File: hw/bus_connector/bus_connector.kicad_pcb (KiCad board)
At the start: 2 copper layers, 70 x 36 mm, 12 parts, among them J1 DB9_Top, J2 DB9_Right, J3 DB9_Left

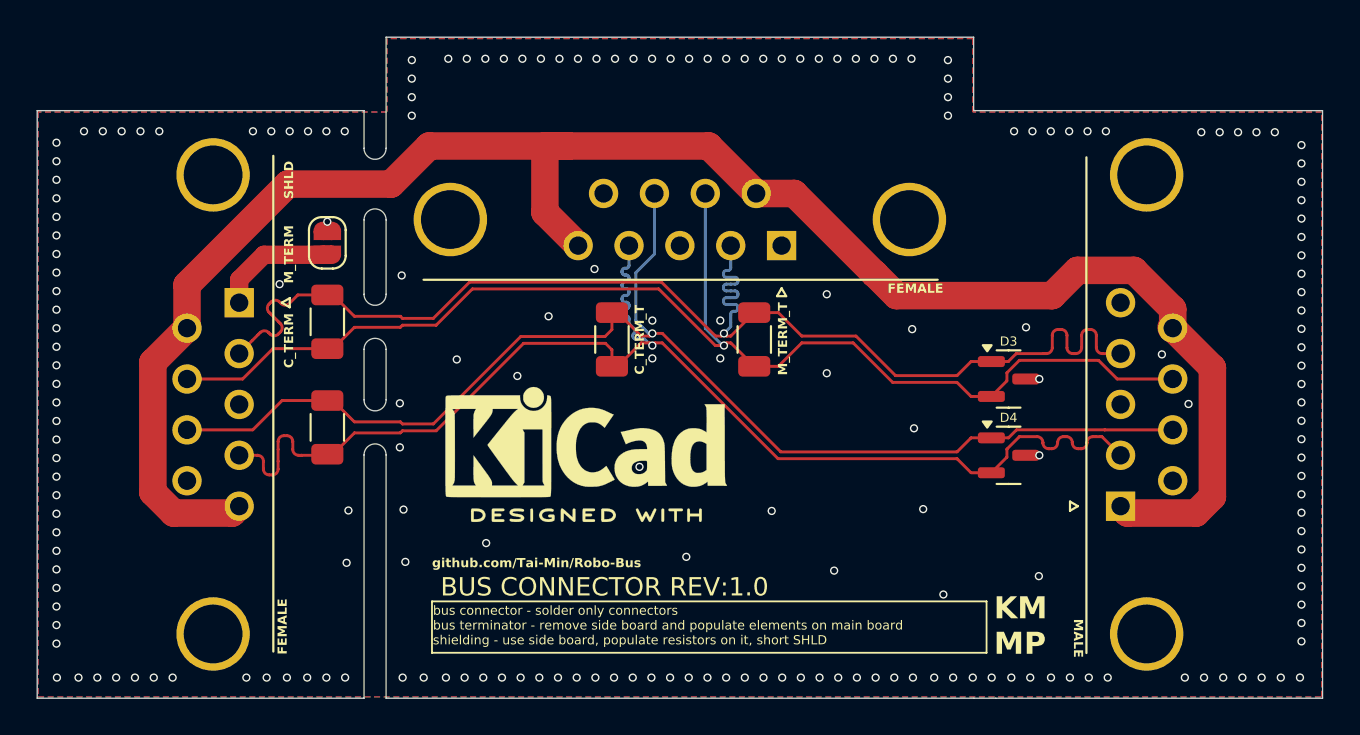
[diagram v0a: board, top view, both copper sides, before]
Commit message: Fix silkscreen, fix thermal error, add via array
Signed-off-by: Mateusz Pająk <22417805+Tai-Min@users.noreply.github.com>
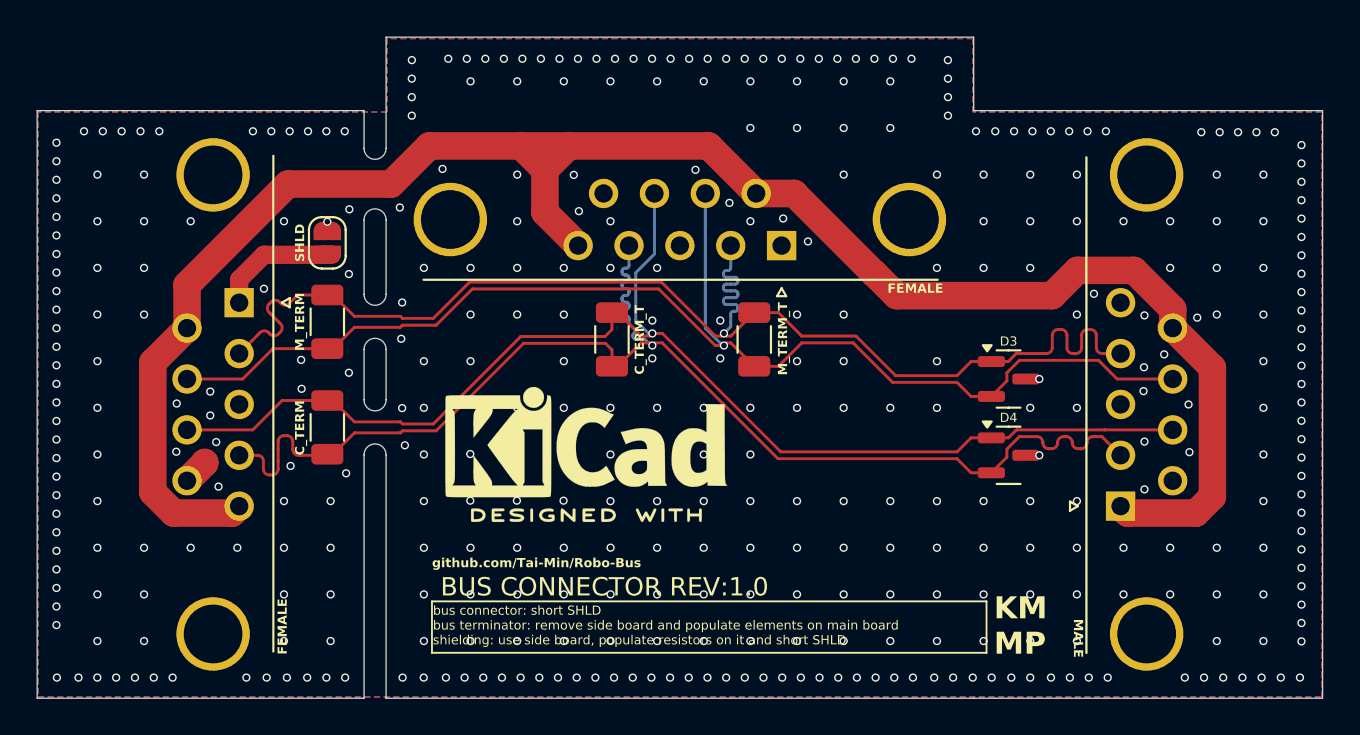
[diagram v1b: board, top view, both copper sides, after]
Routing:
- net GND: track 0.09 -> 1.49 mm, vias 204 -> 397
- net VCC: track 103.5 -> 104.6 mm
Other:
- board text added: "bus connector: short SHLD bus terminator: remove side board and populate elements on main board shielding: use side board, populate resistors on it and short SHLD"
- board text removed: "bus connector - solder only connectors bus terminator - remove side board and populate elements on main board shielding - use side board, populate resistors on it, short SHLD"

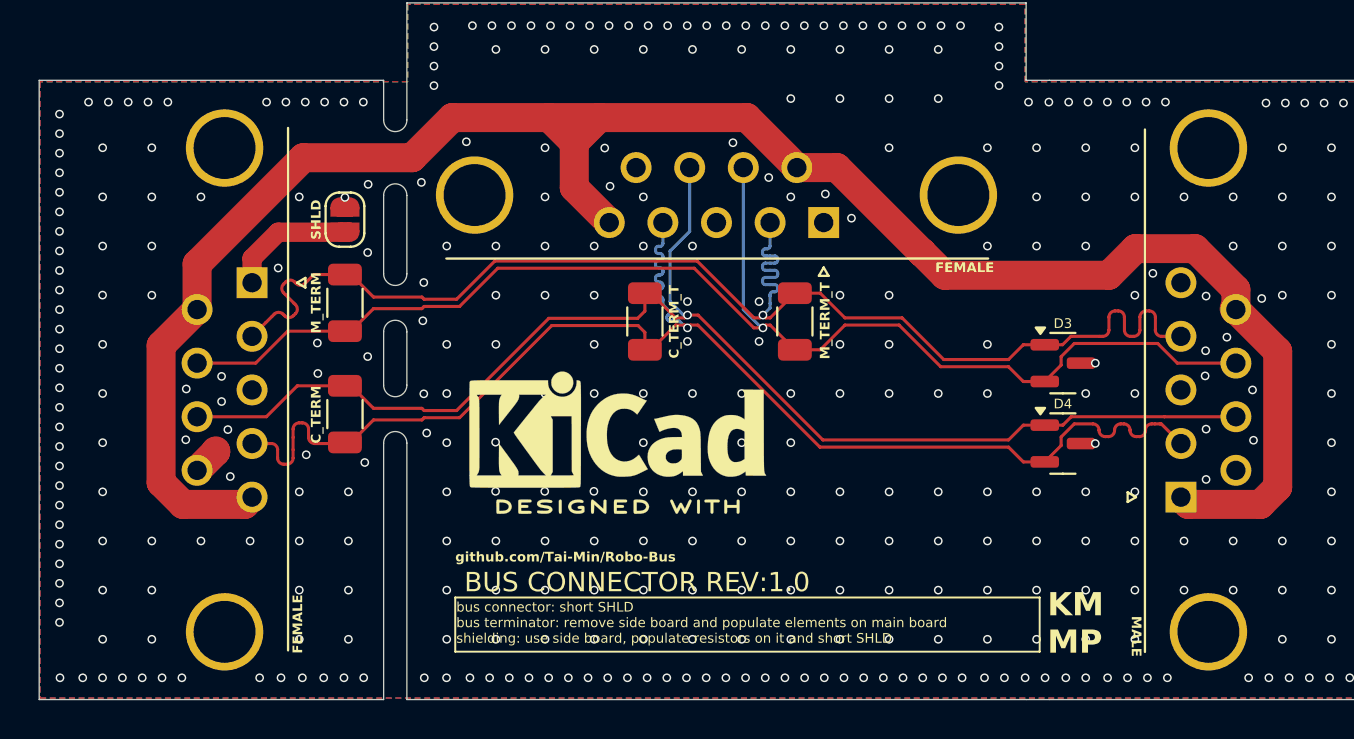
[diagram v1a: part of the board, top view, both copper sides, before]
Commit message: Fix silkscreen
Signed-off-by: Mateusz Pająk <22417805+Tai-Min@users.noreply.github.com>
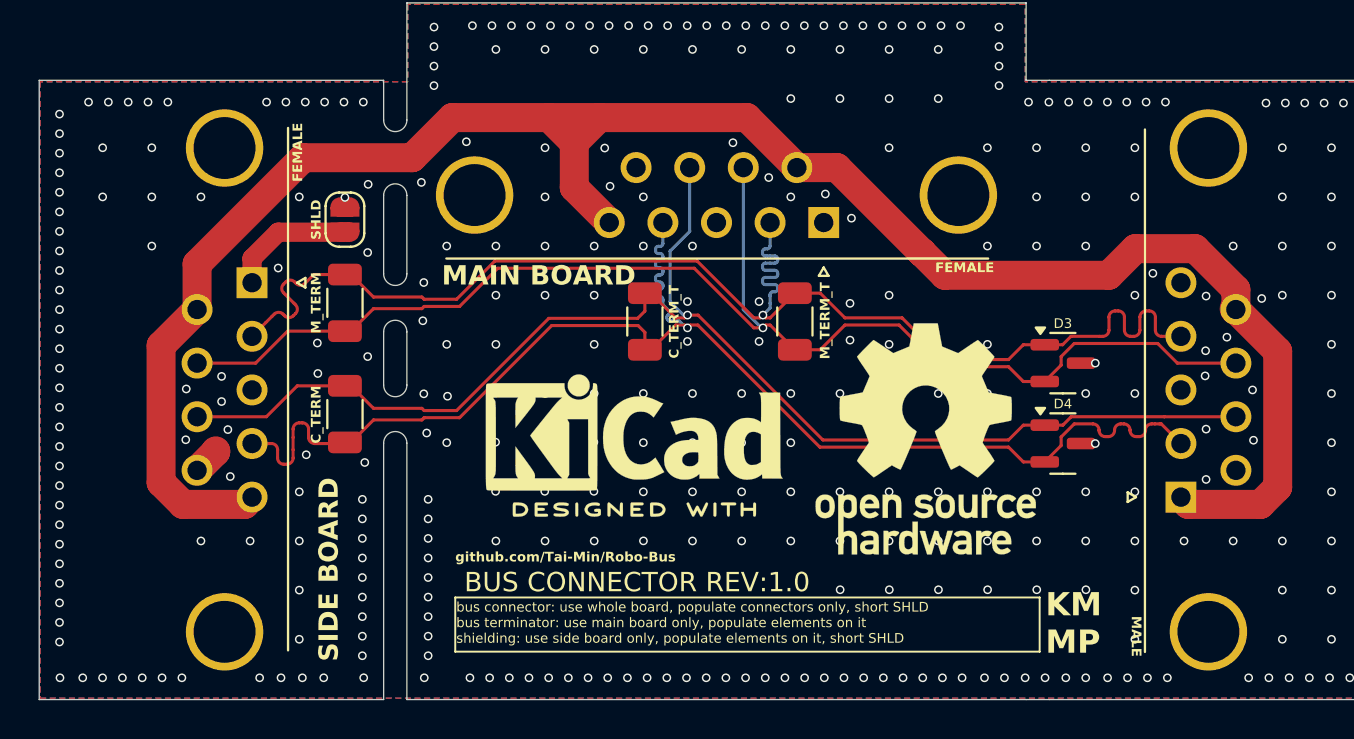
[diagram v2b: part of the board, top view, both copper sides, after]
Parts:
- J1: value DB9_Top -> DE9_Top
- J2: value DB9_Right -> DE9_Right
- J3: value DB9_Left -> DE9_Left
- REF**: moved to F.Cu
- moved REF** 19.2 mm to (157.3, 111.0), turned to 0 degrees
- moved REF** 0.86 mm to (142.2, 110.7)
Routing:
- net GND: vias 397 -> 369
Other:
- board text added: "MAIN BOARD"
- board text added: "SIDE BOARD"
- board text added: "bus connector: use whole board, populate connectors only, short SHLD bus terminator: use main board only, populate elements on it shielding: use side board only, populate elements on it, short SHLD"
- board text removed: "bus connector: short SHLD bus terminator: remove side board and populate elements on main board shielding: use side board, populate resistors on it and short SHLD"

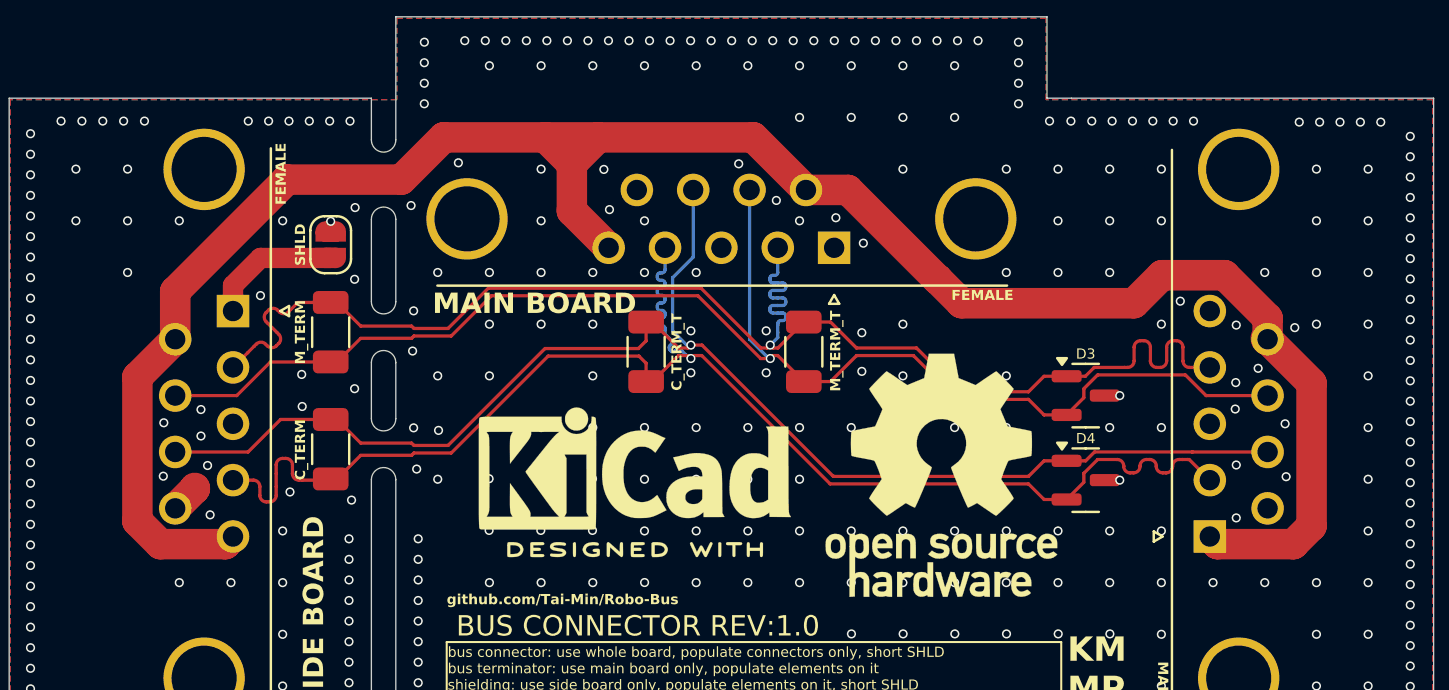
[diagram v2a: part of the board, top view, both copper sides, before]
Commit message: Add datasheets, minor pcb changes
Signed-off-by: Mateusz Pająk <22417805+Tai-Min@users.noreply.github.com>
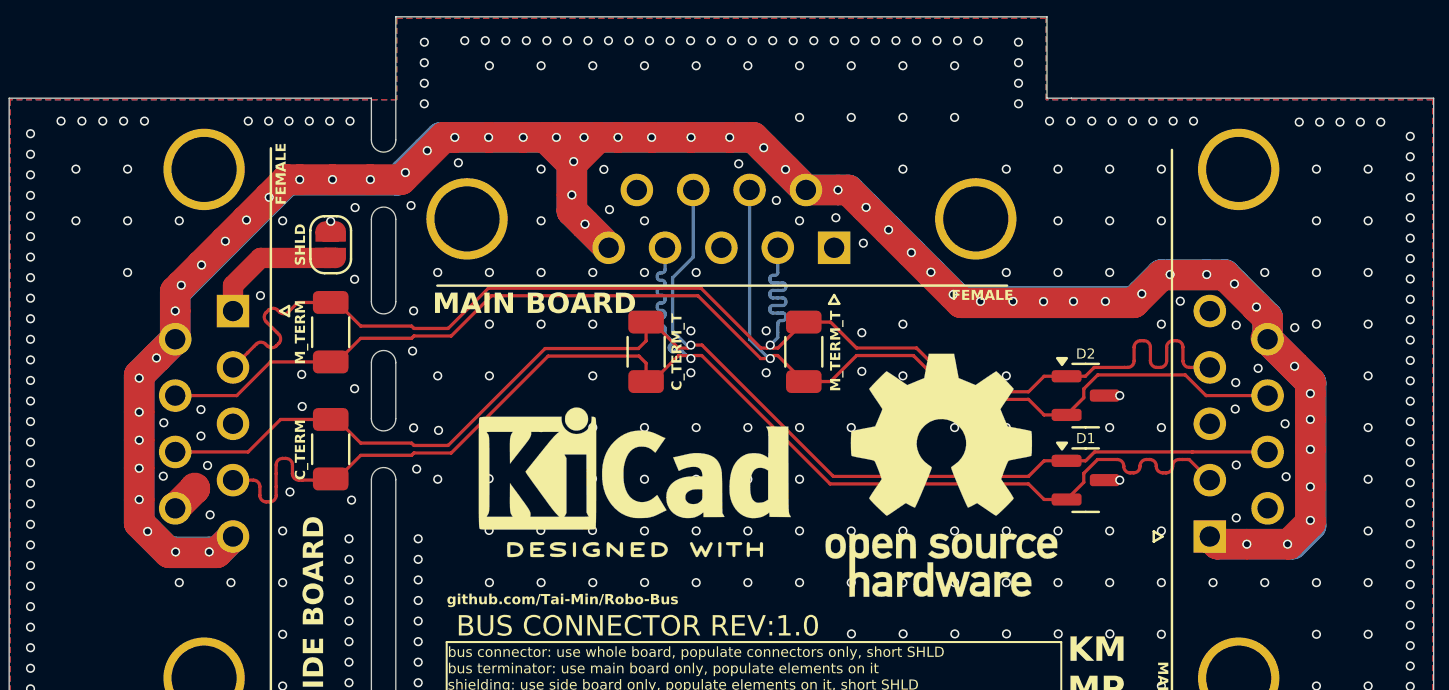
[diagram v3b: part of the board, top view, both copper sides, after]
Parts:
- D2: renamed from D3; value SM712 -> SM712-02HTG
- renumbered D4 to D1, J3 to J1, J1 to J2, J2 to J3
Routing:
- net VCC: track 104.6 -> 209.0 mm, vias 0 -> 58

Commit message: Add  docs
Signed-off-by: Mateusz Pająk <22417805+Tai-Min@users.noreply.github.com>
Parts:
- removed the REF** at (142.2, 110.7)
- added REF**: KiCad-Logo2_5mm_SilkScreen, Symbol:KiCad-Logo2_5mm_SilkScreen, F.Cu at (141.8, 110.9)
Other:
- board text added: "Licensed under CERN OHL v.1.2"
- board text added: "This documentation describes Open Hardware and is licensed under the CERN OHL v. 1.2. You may redistribute and modify this documentation under the terms of the CERN OHL v.1.2.(http://ohwr.org/cernohl). This documentation is distributed WITHOUT ANY EXPRESS OR IMPLIED WARRANTY, INCLUDING OF MERCHANTABILITY, SATISFACTORY QUALITY AND FITNESS FOR A PARTICULAR PURPOSE. Please see the CERN OHL v.1.2 for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"
